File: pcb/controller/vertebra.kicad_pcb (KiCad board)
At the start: 2 copper layers, 20.3 x 46.4 mm, 12 parts, among them J1 AC, J2 CONN_02X10, J3 GND, U1 74LS165

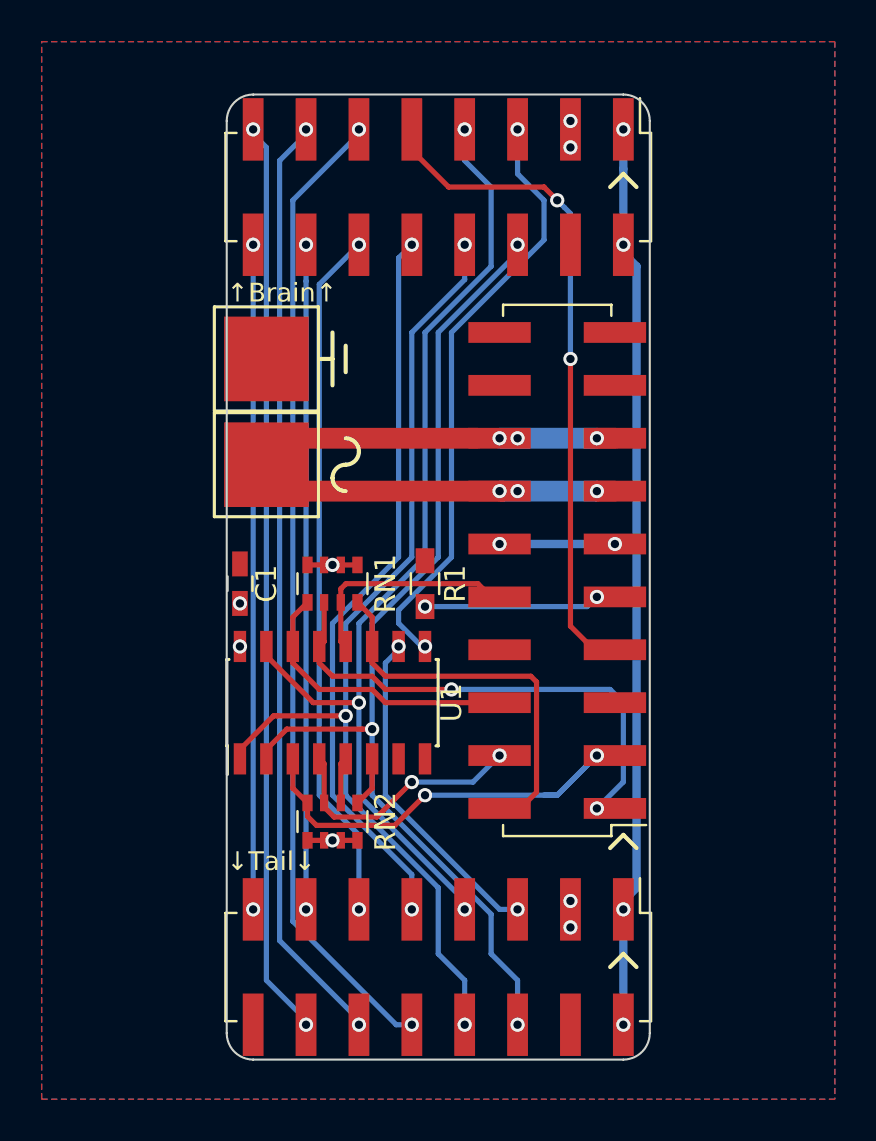
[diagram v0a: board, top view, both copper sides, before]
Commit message: modified vertebra to match brain
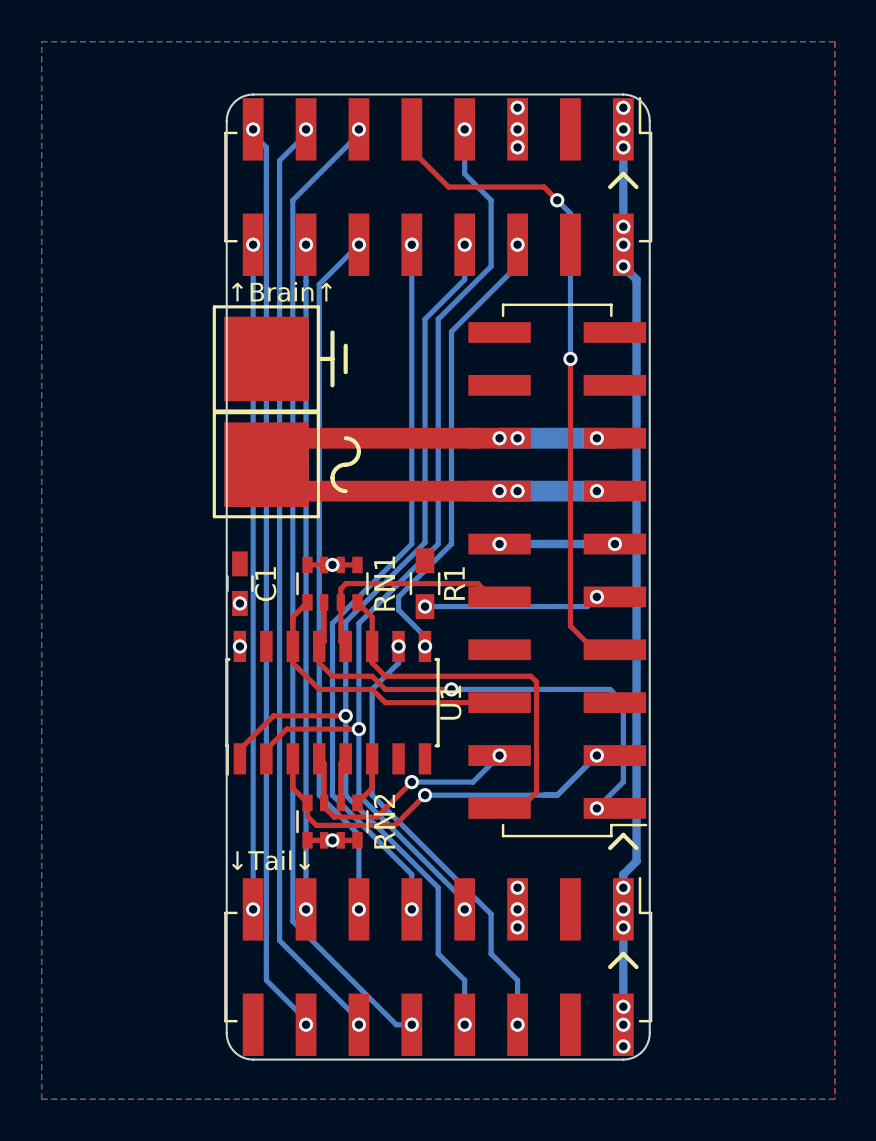
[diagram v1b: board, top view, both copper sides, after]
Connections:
- TO_BRAIN1 pad 3: VCC -> GND
- TO_BRAIN1 pad 5: SERIAL_OUT -> VCC
- TO_BRAIN1 pad 6: CLOCK -> SERIAL_OUT
- TO_BRAIN1 pad 7: ENABLE -> CLOCK
- TO_TAIL1 pad 3: VCC -> GND
- TO_TAIL1 pad 5: SERIAL_IN -> VCC
- TO_TAIL1 pad 6: CLOCK -> SERIAL_IN
- TO_TAIL1 pad 7: ENABLE -> CLOCK
- U1 pad 15: ENABLE -> GND
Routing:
- net ENABLE: track 48.6 -> 0.00 mm, vias 3 -> 0
- net SERIAL_OUT: track 28.9 -> 22.2 mm
- net SERIAL_IN: track 16.0 -> 21.6 mm
- net CLOCK: track 49.2 -> 48.0 mm
- net +12V: track 50.1 -> 51.2 mm, vias 6 -> 14
- net VCC: vias 8 -> 10
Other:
- board text added: "v1.1"
